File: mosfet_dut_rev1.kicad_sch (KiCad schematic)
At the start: 45 parts, among them J2 Conn, J3 Conn_01x02, J4 Conn_01x02, J5 Conn_01x02, J6 Conn_01x02, J7 USB_C_Receptacle_USB2.0_16P, Q1 AO3400A, Q2 AO3400A, Q3 AO3400A, Q4 AO3400A, U2 USBLC6-2SC6, U3 ME6211C33M5, U4 INA219AxD, U5 74HC4051, U6 ESP32-WROOM-32E, U7 CH340C, U8 74HC4051

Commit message: Rev 1.1: Schematic Complete + BOM + JLCPCB Part Numbers
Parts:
- C1, C2, C9: footprint Capacitor_SMD:C_0603_1608Metric -> Capacitor_SMD:C_0805_2012Metric
- J2, J3, J4, J5, J6: footprint TerminalBlock_Phoenix:TerminalBlock_Phoenix_MKDS-1,5-2-5.08_1x02_P5.08mm_Horizontal -> TerminalBlock_Phoenix:TerminalBlock_Phoenix_MKDS-1,5-2_1x02_P5.00mm_Horizontal
- Q1, Q2, Q3, Q4: footprint Package_TO_SOT_SMD:SOT-23 -> Package_TO_SOT_SMD:SOT-23-3
- U5: footprint (none) -> Package_SO:SO-16_3.9x9.9mm_P1.27mm; MFN (none) -> Nexperia – 74HC4051D,652
- U8: footprint (none) -> Package_SO:SO-16_3.9x9.9mm_P1.27mm
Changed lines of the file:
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@@
 	)
 	(junction
+		(at 176.53 129.54)
+		(diameter 0)
+		(color 0 0 0 0)
+	)
+	(junction
 		(at 46.99 34.29)
 		(diameter 0)
@@
 	)
 	(junction
-		(at 176.53 129.54)
-		(diameter 0)
-		(color 0 0 0 0)
-	)
-	(junction
 		(at 191.77 123.19)
 		(diameter 0)
@@
 			)
 		)
-		(property "Footprint" "Package_TO_SOT_SMD:SOT-23"
+		(property "Footprint" "Package_TO_SOT_SMD:SOT-23-3"
 			(at 247.65 94.615 0)
 			(effects
@@
 			)
 		)
-		(property "Footprint" "TerminalBlock_Phoenix:TerminalBlock_Phoenix_MKDS-1,5-2-5.08_1x02_P5.08mm_Horizontal"
+		(property "Footprint" "TerminalBlock_Phoenix:TerminalBlock_Phoenix_MKDS-1,5-2_1x02_P5.00mm_Horizontal"
 			(at 265.43 59.69 0)
 			(effects
@@
 			)
 		)
-		(property "Footprint" "Package_TO_SOT_SMD:SOT-23"
+		(property "Footprint" "Package_TO_SOT_SMD:SOT-23-3"
 			(at 246.38 114.935 0)
 			(effects
@@
 	)
 	(symbol
-		(lib_id "Sensor_Energy:INA219AxD")
-		(at 176.53 139.7 0)
-		(unit 1)
-		(exclude_from_sim no)
-		(in_bom yes)
-		(on_board yes)
-		(dnp no)
-		(fields_autoplaced yes)
-		(property "Reference" "U4"
-			(at 178.6733 127 0)
-			(effects
-				(font
-					(size 1.27 1.27)
-				)
-				(justify left)
-			)
-		)
-		(property "Value" "INA219AxD"
-			(at 178.6733 129.54 0)
-			(effects
-				(font
-					(size 1.27 1.27)
-				)
-				(justify left)
-			)
-		)
-		(property "Footprint" "Package_SO:SOIC-8_3.9x4.9mm_P1.27mm"
-			(at 196.85 148.59 0)
-			(effects
-				(font
-					(size 1.27 1.27)
-				)
-				(hide yes)
-			)
-		)
-		(property "Datasheet" "http://www.ti.com/lit/ds/symlink/ina219.pdf"
-			(at 185.42 142.24 0)
-			(effects
-				(font
-					(size 1.27 1.27)
-				)
-				(hide yes)
-			)
-		)
-		(property "Description" "Zero-Drift, Bidirectional Current/Power Monitor (0-26V) With I2C Interface, SOIC-8"
-			(at 176.53 139.7 0)
-			(effects
-				(font
-					(size 1.27 1.27)
-				)
-				(hide yes)
-			)
-		)
-		(pin "6"
-		)
-		(pin "7"
-		)
-		(pin "3"
-		)
-		(pin "2"
-		)
-		(pin "5"
-		)
-		(pin "4"
-		)
-		(pin "8"
-		)
-		(pin "1"
-		)
-		(instances
-			(project ""
-				(path "/deac0eab-811f-4736-96ff-e9a031bd3138"
-					(reference "U4")
-					(unit 1)
-				)
-			)
-		)
-	)
-	(symbol
 		(lib_id "Device:R")
 		(at 87.63 168.91 0)
@@
 			)
 		)
-		(property "Footprint" "Package_TO_SOT_SMD:SOT-23"
+		(property "Footprint" "Package_TO_SOT_SMD:SOT-23-3"
 			(at 248.92 50.165 0)
 			(effects
@@
 			)
 		)
-		(property "Footprint" "Capacitor_SMD:C_0603_1608Metric"
+		(property "Footprint" "Capacitor_SMD:C_0805_2012Metric"
 			(at 59.3852 27.94 0)
 			(effects
@@
 			)
 		)
-		(property "Footprint" "TerminalBlock_Phoenix:TerminalBlock_Phoenix_MKDS-1,5-2-5.08_1x02_P5.08mm_Horizontal"
+		(property "Footprint" "TerminalBlock_Phoenix:TerminalBlock_Phoenix_MKDS-1,5-2_1x02_P5.00mm_Horizontal"
 			(at 265.43 95.25 0)
 			(effects
@@
 			)
 		)
-		(property "Footprint" "Package_TO_SOT_SMD:SOT-23"
+		(property "Footprint" "Package_TO_SOT_SMD:SOT-23-3"
 			(at 247.65 73.025 0)
 			(effects
@@
 			)
 		)
-		(property "Footprint" "TerminalBlock_Phoenix:TerminalBlock_Phoenix_MKDS-1,5-2-5.08_1x02_P5.08mm_Horizontal"
+		(property "Footprint" "TerminalBlock_Phoenix:TerminalBlock_Phoenix_MKDS-1,5-2_1x02_P5.00mm_Horizontal"
 			(at 265.43 73.66 0)
 			(effects
@@
 			)
 		)
-		(property "Footprint" "TerminalBlock_Phoenix:TerminalBlock_Phoenix_MKDS-1,5-2-5.08_1x02_P5.08mm_Horizontal"
+		(property "Footprint" "TerminalBlock_Phoenix:TerminalBlock_Phoenix_MKDS-1,5-2_1x02_P5.00mm_Horizontal"
 			(at 265.43 116.84 0)
 			(effects
@@
 	)
 	(symbol
+		(lib_id "Sensor_Energy:INA219AxD")
+		(at 176.53 139.7 0)
+		(unit 1)
+		(exclude_from_sim no)
+		(in_bom yes)
+		(on_board yes)
+		(dnp no)
+		(fields_autoplaced yes)
+		(property "Reference" "U4"
+			(at 178.6733 127 0)
+			(effects
+				(font
+					(size 1.27 1.27)
+				)
+				(justify left)
+			)
+		)
+		(property "Value" "INA219AxD"
+			(at 178.6733 129.54 0)
+			(effects
+				(font
+					(size 1.27 1.27)
+				)
+				(justify left)
+			)
+		)
+		(property "Footprint" "Package_SO:SOIC-8_3.9x4.9mm_P1.27mm"
+			(at 196.85 148.59 0)
+			(effects
+				(font
+					(size 1.27 1.27)
+				)
+				(hide yes)
+			)
+		)
+		(property "Datasheet" "http://www.ti.com/lit/ds/symlink/ina219.pdf"
+			(at 185.42 142.24 0)
+			(effects
+				(font
+					(size 1.27 1.27)
+				)
+				(hide yes)
+			)
+		)
+		(property "Description" "Zero-Drift, Bidirectional Current/Power Monitor (0-26V) With I2C Interface, SOIC-8"
+			(at 176.53 139.7 0)
+			(effects
+				(font
+					(size 1.27 1.27)
+				)
+				(hide yes)
+			)
+		)
+		(pin "7"
+		)
+		(pin "6"
+		)
+		(pin "3"
+		)
+		(pin "5"
+		)
+		(pin "4"
+		)
+		(pin "1"
+		)
+		(pin "8"
+		)
+		(pin "2"
+		)
+		(instances
+			(project ""
+				(path "/deac0eab-811f-4736-96ff-e9a031bd3138"
+					(reference "U4")
+					(unit 1)
+				)
+			)
+		)
+	)
+	(symbol
 		(lib_id "Device:R")
 		(at 72.39 168.91 0)
@@
 			)
 		)
-		(property "Footprint" ""
+		(property "Footprint" "Package_SO:SO-16_3.9x9.9mm_P1.27mm"
 			(at 77.47 139.7 0)
 			(effects
@@
 			)
 		)
+		(property "MFN" "Nexperia – 74HC4051D,652"
+			(at 77.47 129.54 0)
+			(effects
+				(font
+					(size 1.27 1.27)
+				)
+				(hide yes)
+			)
+		)
 		(pin "6"
 		)
@@
 			)
 		)
-		(property "Footprint" ""
+		(property "Footprint" "Package_SO:SO-16_3.9x9.9mm_P1.27mm"
 			(at 113.03 139.7 0)
 			(effects
@@
 			)
 		)
-		(property "Footprint" "Capacitor_SMD:C_0603_1608Metric"
+		(property "Footprint" "Capacitor_SMD:C_0805_2012Metric"
 			(at 87.3252 35.56 0)
 			(effects
@@
 			)
 		)
-		(property "Footprint" "TerminalBlock_Phoenix:TerminalBlock_Phoenix_MKDS-1,5-2-5.08_1x02_P5.08mm_Horizontal"
+		(property "Footprint" "TerminalBlock_Phoenix:TerminalBlock_Phoenix_MKDS-1,5-2_1x02_P5.00mm_Horizontal"
 			(at 44.45 144.78 0)
 			(effects
@@
 			)
 		)
-		(property "Footprint" "Capacitor_SMD:C_0603_1608Metric"
+		(property "Footprint" "Capacitor_SMD:C_0805_2012Metric"
 			(at 170.18 27.94 0)
 			(effects

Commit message: Rev 1.1: Colored my nets
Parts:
- added SW1: SW_Push, Button_Switch_SMD:SW_Push_SPST_NO_Alps_SKRK, symbol Switch:SW_Push
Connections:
- net GND: now also SW1.1
- net BOOT renamed UARTDDTR
- net UARTDDTR: now also U6.3 (EN), SW1.2; no longer U6.25 (IO0)
- net ESP32 RX0 renamed UARTDRX
- net ESP32 TX0 renamed UARTDTX
- net RESET renamed UARTDRTS
- net UARTDRTS: now also U6.25 (IO0); no longer U6.3 (EN)
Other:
- note added: "Current Sensor"

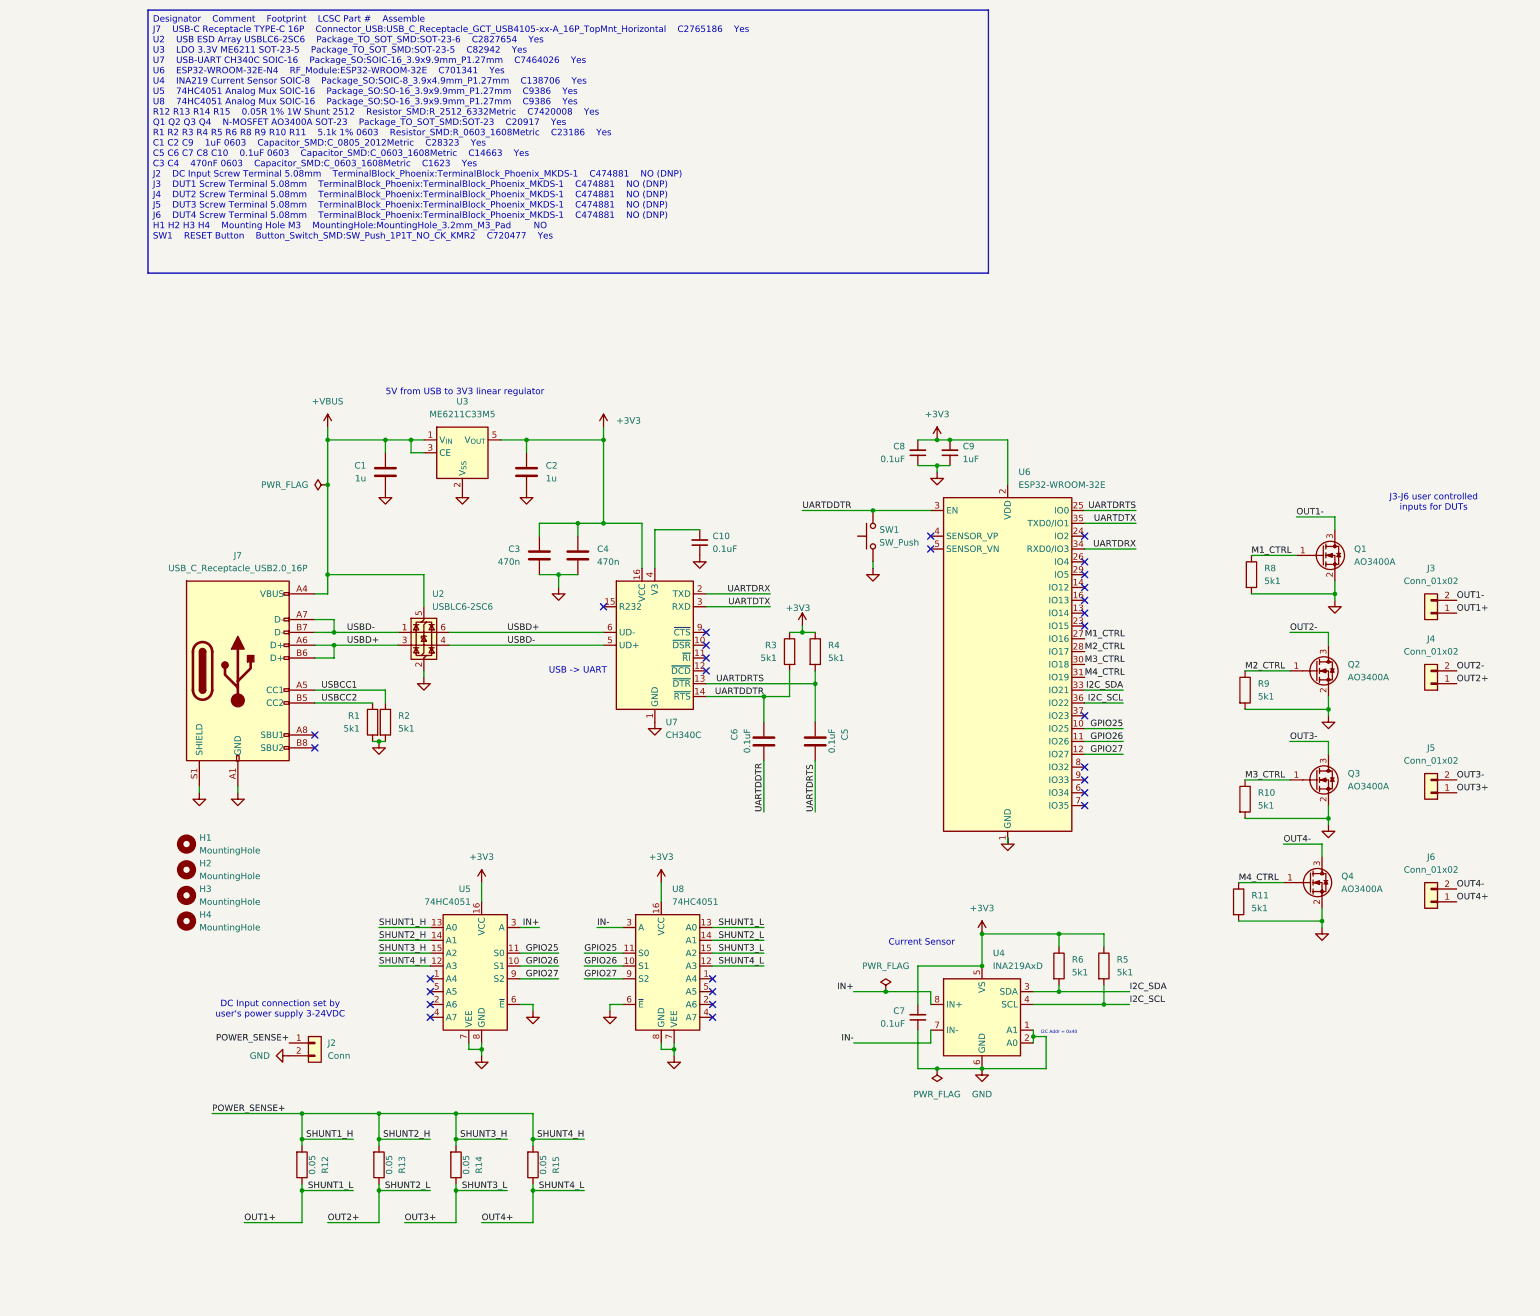
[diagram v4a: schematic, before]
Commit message: Rev 1.1: Final Component Schematic + BOM
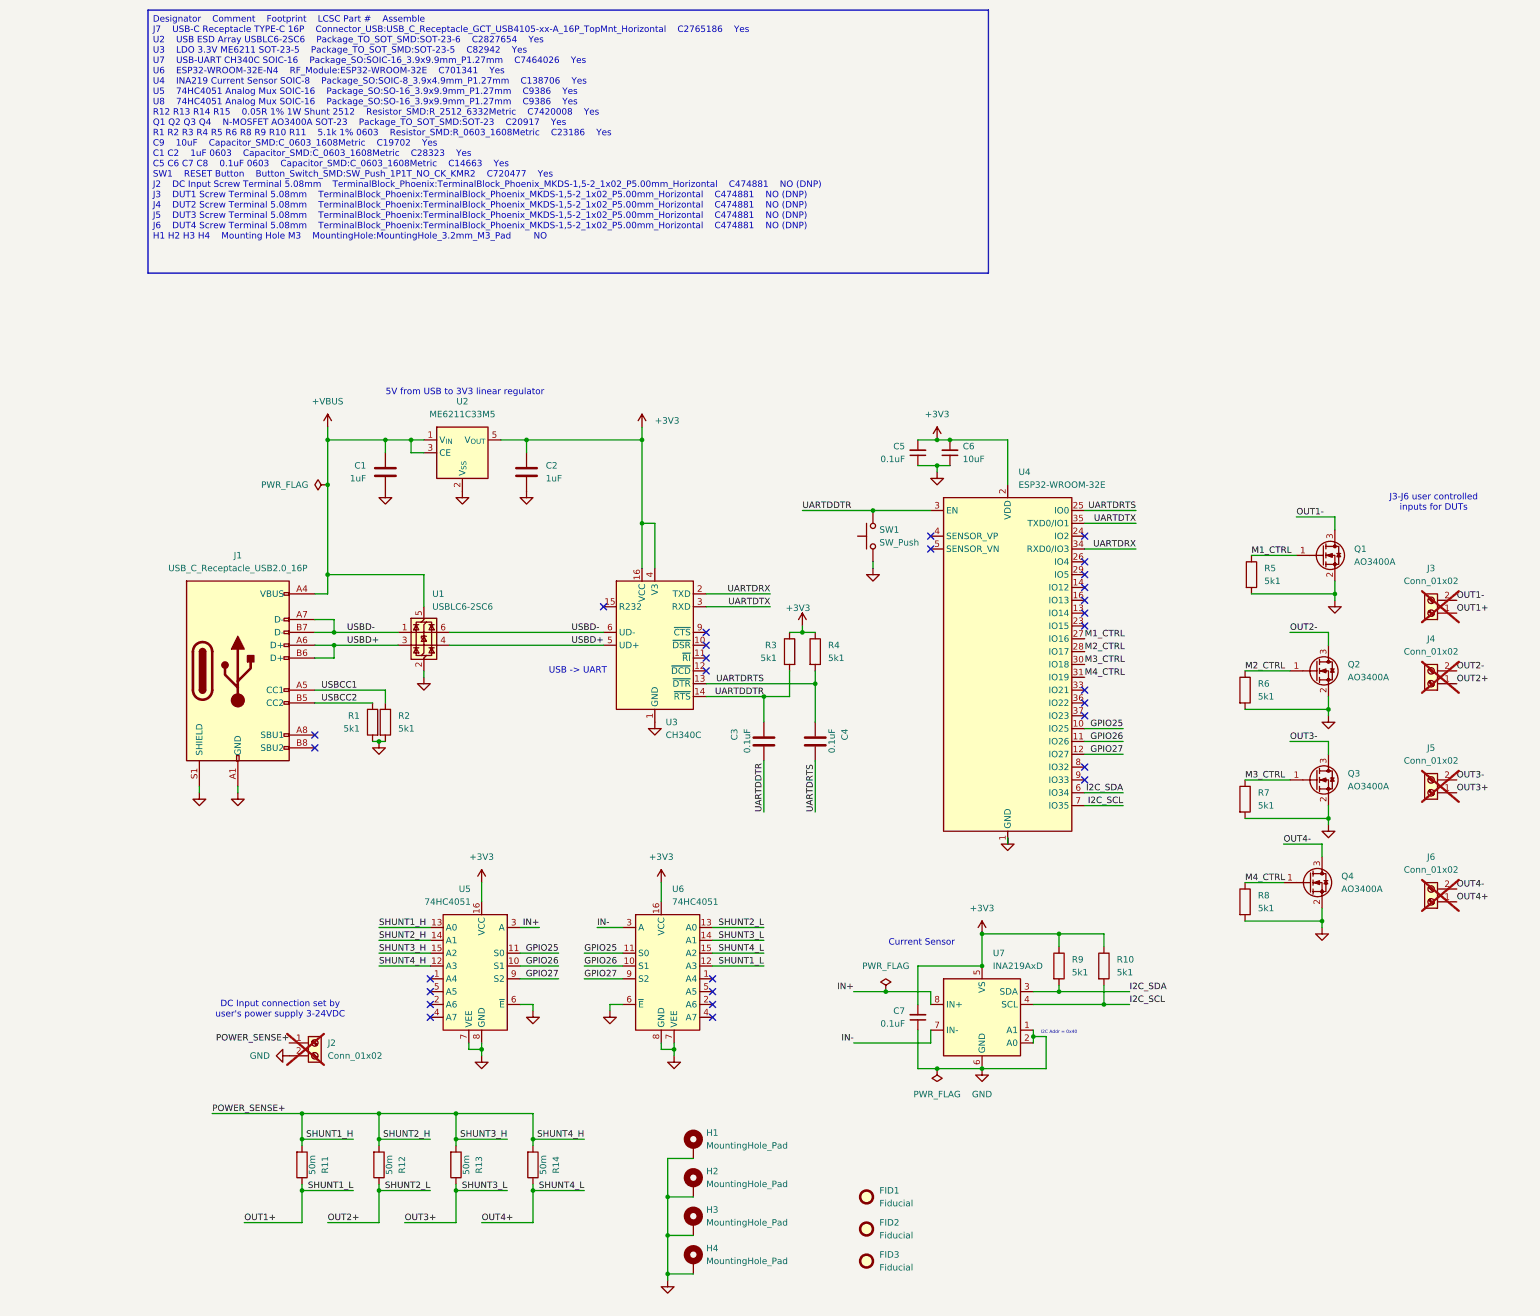
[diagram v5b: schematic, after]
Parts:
- removed C10: 0.1uF, Capacitor_SMD:C_0603_1608Metric, symbol Device:C_Small
- removed C3, C4: 470n, Capacitor_SMD:C_0603_1608Metric, symbol Device:C
- removed H1, H2, H3, H4: MountingHole, MountingHole:MountingHole_3.2mm_M3_Pad, symbol Mechanical:MountingHole
- added FID1, FID2, FID3: Fiducial, Fiducial:Fiducial_1mm_Mask2mm, symbol Mechanical:Fiducial
- added H1, H2, H3, H4: MountingHole_Pad, MountingHole:MountingHole_2.7mm_Pad_Via, symbol Mechanical:MountingHole_Pad
- C1, C2: value 1u -> 1uF; footprint Capacitor_SMD:C_0805_2012Metric -> Capacitor_SMD:C_0603_1608Metric; JLCPCB Part # (none) -> C28323
- C3: renamed from C6; JLCPCB Part # (none) -> C14663
- C4: renamed from C5; JLCPCB Part # (none) -> C14663
- C5: renamed from C8; JLCPCB Part # (none) -> C14663
- C6: renamed from C9; value 1uF -> 10uF; footprint Capacitor_SMD:C_0805_2012Metric -> Capacitor_SMD:C_0603_1608Metric; JLCPCB Part # (none) -> C19702
- C7: JLCPCB Part # (none) -> C14663
- J1: renamed from J7; JLCPCB Part # (none) -> C2765186
- J2: value Conn -> Conn_01x02; symbol Connector_Generic:Conn_01x02 -> Connector:Screw_Terminal_01x02; JLCPCB Part # (none) -> C474881; now not fitted
- J3, J4, J5, J6: symbol Connector_Generic:Conn_01x02 -> Connector:Screw_Terminal_01x02; JLCPCB Part # (none) -> C474881; now not fitted
- Q1, Q2, Q3, Q4: JLCPCB Part # (none) -> C20917
- R1, R2, R3, R4: JLCPCB Part # (none) -> C23186
- R10: renamed from R5; JLCPCB Part # (none) -> C23186
- R11: renamed from R12; value 0.05 -> 50m; JLCPCB Part # (none) -> C7420008
- R12: renamed from R13; value 0.05 -> 50m; JLCPCB Part # (none) -> C7420008
- R13: renamed from R14; value 0.05 -> 50m; JLCPCB Part # (none) -> C7420008
- R14: renamed from R15; value 0.05 -> 50m; JLCPCB Part # (none) -> C7420008
- R5: renamed from R8; JLCPCB Part # (none) -> C23186
- R6: renamed from R9; JLCPCB Part # (none) -> C23186
- R7: renamed from R10; JLCPCB Part # (none) -> C23186
- R8: renamed from R11; JLCPCB Part # (none) -> C23186
- R9: renamed from R6; JLCPCB Part # (none) -> C23186
- SW1: JLCPCB Part # (none) -> C720477
- U1: renamed from U2; JLCPCB Part # (none) -> C2827654
- U2: renamed from U3; JLCPCB Part # (none) -> C82942
- U3: renamed from U7; JLCPCB Part # (none) -> C7464026
- U4: renamed from U6; JLCPCB Part # (none) -> C701341
- U5: JLCPCB Part # (none) -> C9386
- U6: renamed from U8; JLCPCB Part # (none) -> C9386
- U7: renamed from U4; JLCPCB Part # (none) -> C138706
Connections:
- net +3V3: now also U3.4 (V3)
- net GND: now also H1.1, H2.1, H3.1, H4.1
- net I2C_SCL: now also U4.7 (IO35); no longer U4.36 (IO22)
- net I2C_SDA: now also U4.6 (IO34); no longer U4.33 (IO21)
- net OUT1+: now also U6.12 (A3); no longer U6.13 (A0)
- net OUT2+: now also U6.13 (A0); no longer U6.14 (A1)
- net OUT3+: now also U6.14 (A1); no longer U6.15 (A2)
- net OUT4+: now also U6.15 (A2); no longer U6.12 (A3)
- net USBD+: now also U1.4 (I/O2), U3.5 (UD+); no longer U1.6 (I/O1), U3.6 (UD-)
- net USBD-: now also U1.6 (I/O1), U3.6 (UD-); no longer U1.4 (I/O2), U3.5 (UD+)
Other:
- moved on the sheet: R8

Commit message: Rev 1.1: Board placement and rough tracks
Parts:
- removed U5: 74HC4051, Package_SO:SO-16_3.9x9.9mm_P1.27mm, symbol 74xx:74HC4051
- renumbered U6 to U5, U7 to U6
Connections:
- net IN+ is gone; now on net POWER_SENSE+: U6.8 (IN+)
- net I2C_SCL: now also U4.6 (IO34); no longer U4.7 (IO35)
- net I2C_SDA: now also U4.7 (IO35); no longer U4.6 (IO34)
- net M1_CTRL: now also U4.31 (IO19); no longer U4.27 (IO16)
- net M2_CTRL: now also U4.30 (IO18); no longer U4.28 (IO17)
- net M3_CTRL: now also U4.28 (IO17); no longer U4.30 (IO18)
- net M4_CTRL: now also U4.27 (IO16); no longer U4.31 (IO19)
- net OUT1+: now also U5.5 (A5); no longer U5.12 (A3)
- net OUT2+: now also U5.4 (A7); no longer U5.13 (A0)
- net OUT3+: now also U5.2 (A6); no longer U5.14 (A1)
- net OUT4+: now also U5.1 (A4); no longer U5.15 (A2)
- net USBD+: no longer J1.A6 (D+), J1.B6 (D+), U1.3 (I/O2)
- net USBD-: no longer J1.A7 (D-), J1.B7 (D-), U1.1 (I/O1)
- new net USBCD+: J1.A6 (D+), J1.B6 (D+), U1.3 (I/O2)
- new net USBCD-: J1.A7 (D-), J1.B7 (D-), U1.1 (I/O1)
- no-connect marks 29 -> 25
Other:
- moved on the sheet: U5

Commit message: Rev 1.1: Final
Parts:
- C1, C2: JLCPCB Part # C28323 -> CL10A105KB8NNNC
- FID1, FID2, FID3: now in the parts list
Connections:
- net UARTDDTR: no longer C3.2, R3.2, SW1.2, U4.3 (EN)
- net UARTDRTS: no longer C4.1, R4.2, U4.25 (IO0)
- new net UARTDDTR_EN: C3.2, R4.2, SW1.2, U4.3 (EN)
- new net UARTDRTS_IO0: C4.1, R3.2, U4.25 (IO0)
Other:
- moved on the sheet: C3, C4, R3, R4
